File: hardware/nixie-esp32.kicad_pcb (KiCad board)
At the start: 6 copper layers, 70.5 x 70 mm, 53 parts, among them J1 USB4216-03-A_REVA, SW1 RESET, SW2 BOOT, U1 AP7361C-33E-13, U2 ESP32-S3-WROOM-1, U3 SN74AHCT1G125DBVR, U4 SN74141N, U5 SN74141N, U6 SN74141N

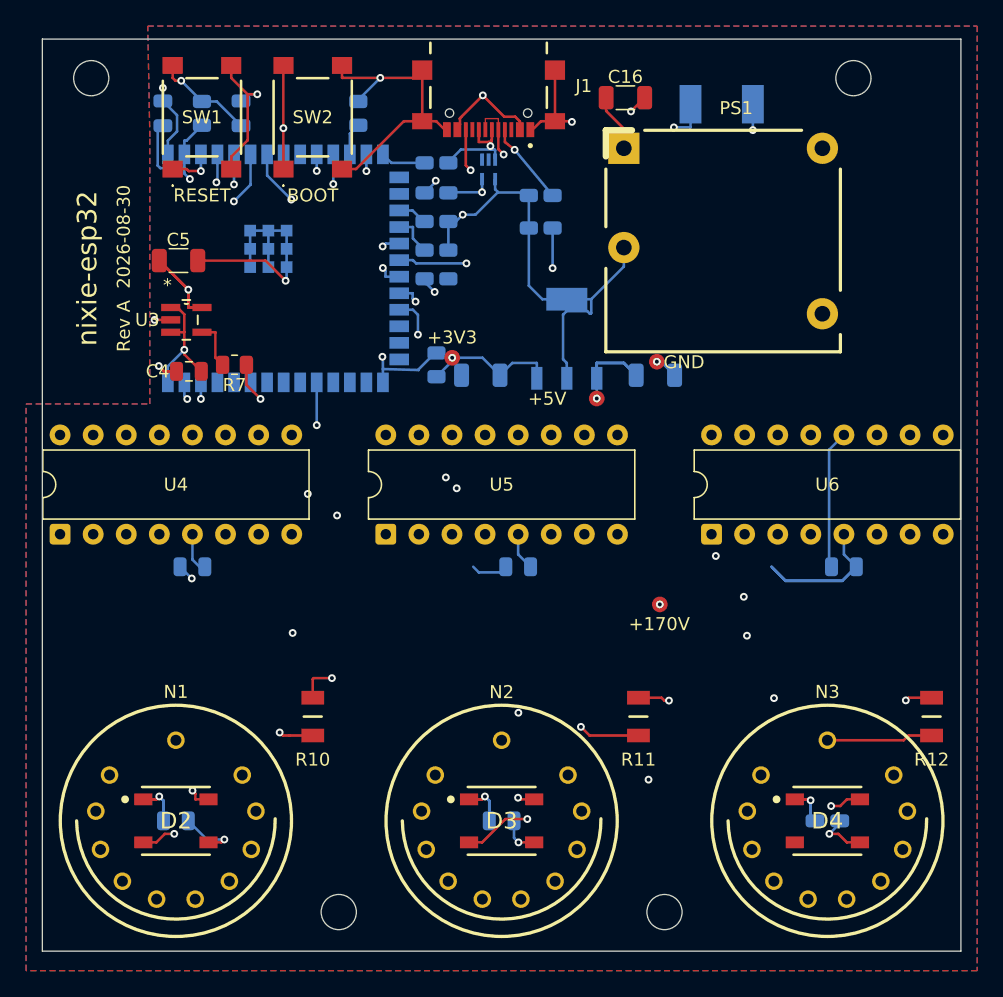
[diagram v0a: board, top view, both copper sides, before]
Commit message: Resolve all DRC warnings
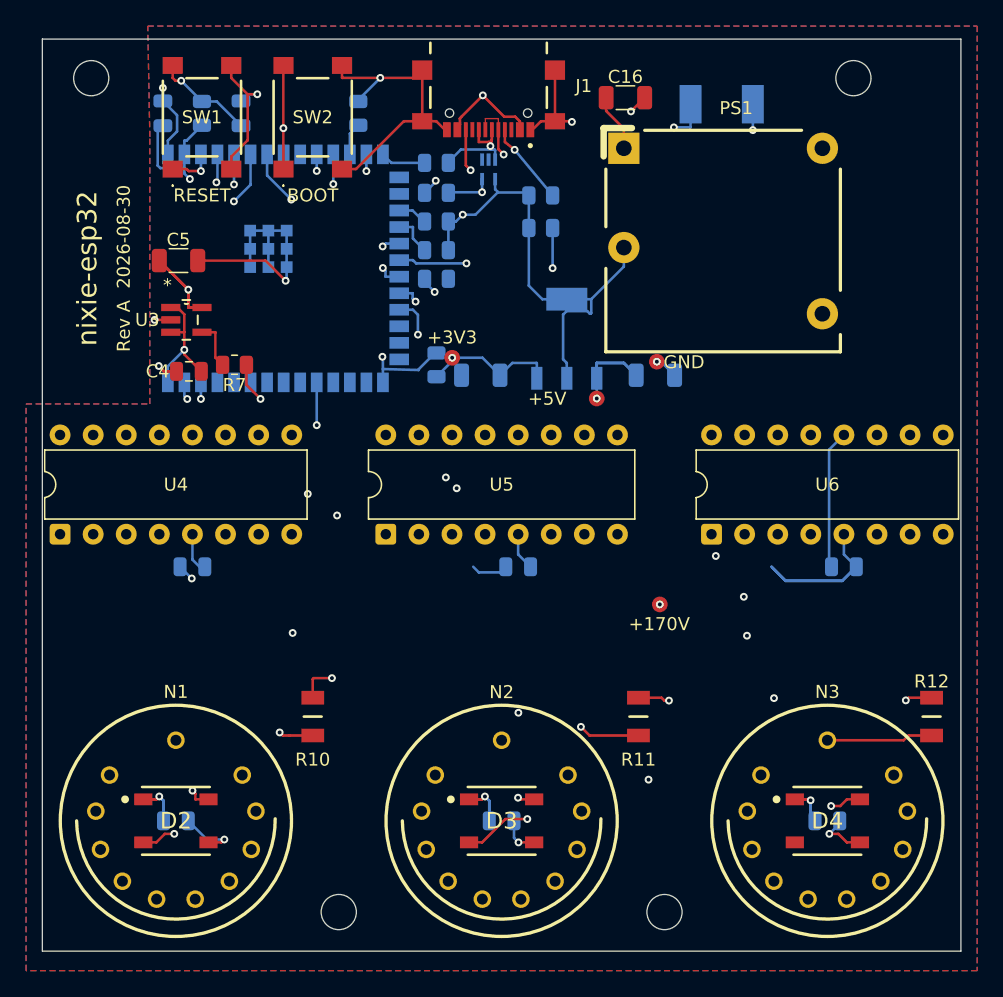
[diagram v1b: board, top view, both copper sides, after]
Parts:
- U4, U6: footprint Package_DIP:DIP-16_W7.62mm -> nixie-esp32:DIP-16_W7.62mm
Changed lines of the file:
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@@
 		(duplicate_pad_numbers_are_jumpers no)
 		(fp_line
-			(start -1.38 -1.38)
-			(end -1.38 0.62)
+			(start -1.55 -1.55)
+			(end -1.55 0.62)
 			(stroke
 				(width 0.5)
@@
 		)
 		(fp_line
-			(start -1.38 -1.38)
-			(end 0.62 -1.38)
+			(start -1.55 -1.55)
+			(end 0.62 -1.55)
 			(stroke
 				(width 0.5)
@@
 		)
 	)
-	(footprint "Package_DIP:DIP-16_W7.62mm"
+	(footprint "nixie-esp32:DIP-16_W7.62mm"
 		(layer "F.Cu")
 		(at 170.11 114.5 90)
@@
 		(duplicate_pad_numbers_are_jumpers no)
 		(fp_line
-			(start 6.46 -1.33)
-			(end 4.81 -1.33)
+			(start 6.46 -1.18)
+			(end 4.81 -1.18)
 			(stroke
 				(width 0.12)
@@
 		)
 		(fp_line
-			(start 2.81 -1.33)
-			(end 1.16 -1.33)
+			(start 2.81 -1.18)
+			(end 1.16 -1.18)
 			(stroke
 				(width 0.12)
@@
 		)
 		(fp_line
-			(start 1.16 -1.33)
-			(end 1.16 19.11)
+			(start 1.16 -1.18)
+			(end 1.16 18.96)
 			(stroke
 				(width 0.12)
@@
 		)
 		(fp_line
-			(start 6.46 19.11)
-			(end 6.46 -1.33)
+			(start 6.46 18.96)
+			(end 6.46 -1.18)
 			(stroke
 				(width 0.12)
@@
 		)
 		(fp_line
-			(start 1.16 19.11)
-			(end 6.46 19.11)
+			(start 1.16 18.96)
+			(end 6.46 18.96)
 			(stroke
 				(width 0.12)
@@
 		)
 		(fp_arc
-			(start 4.81 -1.33)
+			(start 4.81 -1.18)
 			(mid 3.81 -0.33)
-			(end 2.81 -1.33)
+			(end 2.81 -1.18)
 			(stroke
 				(width 0.12)
@@
 		)
 	)
-	(footprint "Package_DIP:DIP-16_W7.62mm"
+	(footprint "nixie-esp32:DIP-16_W7.62mm"
 		(layer "F.Cu")
 		(at 120.11 114.5 90)
@@
 		(duplicate_pad_numbers_are_jumpers no)
 		(fp_line
-			(start 6.46 -1.33)
-			(end 4.81 -1.33)
+			(start 6.46 -1.18)
+			(end 4.81 -1.18)
 			(stroke
 				(width 0.12)
@@
 		)
 		(fp_line
-			(start 2.81 -1.33)
-			(end 1.16 -1.33)
+			(start 2.81 -1.18)
+			(end 1.16 -1.18)
 			(stroke
 				(width 0.12)
@@
 		)
 		(fp_line
-			(start 1.16 -1.33)
-			(end 1.16 19.11)
+			(start 1.16 -1.18)
+			(end 1.16 18.96)
 			(stroke
 				(width 0.12)
@@
 		)
 		(fp_line
-			(start 6.46 19.11)
-			(end 6.46 -1.33)
+			(start 6.46 18.96)
+			(end 6.46 -1.18)
 			(stroke
 				(width 0.12)
@@
 		)
 		(fp_line
-			(start 1.16 19.11)
-			(end 6.46 19.11)
+			(start 1.16 18.96)
+			(end 6.46 18.96)
 			(stroke
 				(width 0.12)
@@
 		)
 		(fp_arc
-			(start 4.81 -1.33)
+			(start 4.81 -1.18)
 			(mid 3.81 -0.33)
-			(end 2.81 -1.33)
+			(end 2.81 -1.18)
 			(stroke
 				(width 0.12)
@@
 		(tags "Resistor")
 		(property "Reference" "R12"
-			(at -3.3 0 0)
+			(at 2.7 0 0)
 			(layer "F.SilkS")
 			(effects
@@
 		)
 		(pad "1" smd roundrect
-			(at -0.95 0 270)
+			(at -0.95 0 90)
 			(size 1 1.45)
 			(layers "B.Cu" "B.Mask" "B.Paste")
@@
 		)
 		(pad "2" smd roundrect
-			(at 0.95 0 270)
+			(at 0.95 0 90)
 			(size 1 1.45)
 			(layers "B.Cu" "B.Mask" "B.Paste")
@@
 		)
 		(pad "1" smd roundrect
-			(at -0.95 0 180)
+			(at -0.95 0)
 			(size 1 1.45)
 			(layers "B.Cu" "B.Mask" "B.Paste")
@@
 		)
 		(pad "2" smd roundrect
-			(at 0.95 0 180)
+			(at 0.95 0)
 			(size 1 1.45)
 			(layers "B.Cu" "B.Mask" "B.Paste")
@@
 		(tags "capacitor")
 		(property "Reference" "C12"
-			(at 0 1.68 0)
+			(at -3.43 0 0)
 			(layer "B.SilkS")
 			(effects
@@
 		(tags "capacitor")
 		(property "Reference" "C11"
-			(at 0 1.68 0)
+			(at -3.429999 0 0)
 			(layer "B.SilkS")
 			(effects
@@
 		(tags "resistor")
 		(property "Reference" "R6"
-			(at -1.5 2.3 0)
+			(at -2.4 0 0)
 			(layer "B.SilkS")
 			(effects
@@
 		)
 		(pad "1" smd roundrect
-			(at -0.9125 0 270)
+			(at -0.9125 0 90)
 			(size 1.025 1.4)
 			(layers "B.Cu" "B.Mask" "B.Paste")
@@
 		)
 		(pad "2" smd roundrect
-			(at 0.9125 0 270)
+			(at 0.9125 0 90)
 			(size 1.025 1.4)
 			(layers "B.Cu" "B.Mask" "B.Paste")
@@
 		)
 		(pad "1" smd roundrect
-			(at -0.9125 0 270)
+			(at -0.9125 0)
 			(size 1.025 1.4)
 			(layers "B.Cu" "B.Mask" "B.Paste")
@@
 		)
 		(pad "2" smd roundrect
-			(at 0.9125 0 270)
+			(at 0.9125 0)
 			(size 1.025 1.4)
 			(layers "B.Cu" "B.Mask" "B.Paste")
@@
 		)
 		(pad "1" smd roundrect
-			(at -0.95 0 270)
+			(at -0.95 0)
 			(size 1 1.45)
 			(layers "B.Cu" "B.Mask" "B.Paste")
@@
 		)
 		(pad "2" smd roundrect
-			(at 0.95 0 270)
+			(at 0.95 0)
 			(size 1 1.45)
 			(layers "B.Cu" "B.Mask" "B.Paste")
@@
 		)
 		(pad "1" smd roundrect
-			(at -0.9125 0 270)
+			(at -0.9125 0)
 			(size 1.025 1.4)
 			(layers "B.Cu" "B.Mask" "B.Paste")
@@
 		)
 		(pad "2" smd roundrect
-			(at 0.9125 0 270)
+			(at 0.9125 0)
 			(size 1.025 1.4)
 			(layers "B.Cu" "B.Mask" "B.Paste")
@@
 		)
 		(pad "1" smd roundrect
-			(at -0.95 0 270)
+			(at -0.95 0 90)
 			(size 1 1.45)
 			(layers "B.Cu" "B.Mask" "B.Paste")
@@
 		)
 		(pad "2" smd roundrect
-			(at 0.95 0 270)
+			(at 0.95 0 90)
 			(size 1 1.45)
 			(layers "B.Cu" "B.Mask" "B.Paste")
@@
 		)
 		(pad "1" smd roundrect
-			(at -0.9125 0 90)
+			(at -0.9125 0)
 			(size 1.025 1.4)
 			(layers "B.Cu" "B.Mask" "B.Paste")
@@
 		)
 		(pad "2" smd roundrect
-			(at 0.9125 0 90)
+			(at 0.9125 0)
 			(size 1.025 1.4)
 			(layers "B.Cu" "B.Mask" "B.Paste")
@@
 			(polygon
 				(pts
-					(xy 126.84 103.1) (xy 126.84 85.1) (xy 117.5 85.1) (xy 117.5 103.1)
+					(xy 126.84 103.1) (xy 126.84 85.1) (xy 120.89 85.1) (xy 120.89 103.1)
 				)
 			)
@@
 		(tags "capacitor")
 		(property "Reference" "C13"
-			(at 0 1.68 0)
+			(at -3.43 0 0)
 			(layer "B.SilkS")
 			(effects
@@
 		)
 		(pad "1" smd roundrect
-			(at -0.95 0 180)
+			(at -0.95 0)
 			(size 1 1.45)
 			(layers "B.Cu" "B.Mask" "B.Paste")
@@
 		)
 		(pad "2" smd roundrect
-			(at 0.95 0 180)
+			(at 0.95 0)
 			(size 1 1.45)
 			(layers "B.Cu" "B.Mask" "B.Paste")
@@
 		)
 		(pad "1" smd roundrect
-			(at -0.9125 0 270)
+			(at -0.9125 0 90)
 			(size 1.025 1.4)
 			(layers "B.Cu" "B.Mask" "B.Paste")
@@
 		)
 		(pad "2" smd roundrect
-			(at 0.9125 0 270)
+			(at 0.9125 0 90)
 			(size 1.025 1.4)
 			(layers "B.Cu" "B.Mask" "B.Paste")
@@
 		)
 		(pad "1" smd roundrect
-			(at -1.475 0 180)
+			(at -1.475 0)
 			(size 1.15 1.8)
 			(layers "B.Cu" "B.Mask" "B.Paste")
@@
 		)
 		(pad "2" smd roundrect
-			(at 1.475 0 180)
+			(at 1.475 0)
 			(size 1.15 1.8)
 			(layers "B.Cu" "B.Mask" "B.Paste")
@@
 		)
 		(pad "1" smd roundrect
-			(at -0.9125 0 90)
+			(at -0.9125 0)
 			(size 1.025 1.4)
 			(layers "B.Cu" "B.Mask" "B.Paste")
@@
 		)
 		(pad "2" smd roundrect
-			(at 0.9125 0 90)
+			(at 0.9125 0)
 			(size 1.025 1.4)
 			(layers "B.Cu" "B.Mask" "B.Paste")
@@
 		)
 		(pad "1" smd roundrect
-			(at -0.9125 0 90)
+			(at -0.9125 0)
 			(size 1.025 1.4)
 			(layers "B.Cu" "B.Mask" "B.Paste")
@@
 		)
 		(pad "2" smd roundrect
-			(at 0.9125 0 90)
+			(at 0.9125 0)
 			(size 1.025 1.4)
 			(layers "B.Cu" "B.Mask" "B.Paste")
@@
 		)
 		(pad "1" smd roundrect
-			(at -0.9125 0 270)
+			(at -0.9125 0)
 			(size 1.025 1.4)
 			(layers "B.Cu" "B.Mask" "B.Paste")
@@
 		)
 		(pad "2" smd roundrect
-			(at 0.9125 0 270)
+			(at 0.9125 0)
 			(size 1.025 1.4)
 			(layers "B.Cu" "B.Mask" "B.Paste")
@@
 		)
 		(pad "1" smd roundrect
-			(at -0.9125 0 90)
+			(at -0.9125 0)
 			(size 1.025 1.4)
 			(layers "B.Cu" "B.Mask" "B.Paste")
@@
 		)
 		(pad "2" smd roundrect
-			(at 0.9125 0 90)
+			(at 0.9125 0)
 			(size 1.025 1.4)
 			(layers "B.Cu" "B.Mask" "B.Paste")
@@
 			)
 		)
+	)
+	(zone
+		(layers "F.Cu" "B.Cu" "In1.Cu" "In2.Cu" "In3.Cu" "In4.Cu")
+		(name "antenna keepout to board edge")
+		(hatch edge 0.5)
+		(connect_pads
+			(clearance 0)
+		)
+		(min_thickness 0.25)
+		(keepout
+			(tracks not_allowed)
+			(vias not_allowed)
+			(pads not_allowed)
+			(copperpour not_allowed)
+			(footprints allowed)
+		)
+		(placement
+			(enabled no)
+			(sheetname "")
+		)
+		(fill
+			(thermal_gap 0.5)
+			(thermal_bridge_width 0.5)
+			(island_removal_mode 0)
+		)
+		(polygon
+			(pts
+				(xy 117.5 85.1) (xy 120.89 85.1) (xy 120.89 103.1) (xy 117.5 103.1)
+			)
+		)

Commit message: Add component values and context labels to silkscreen
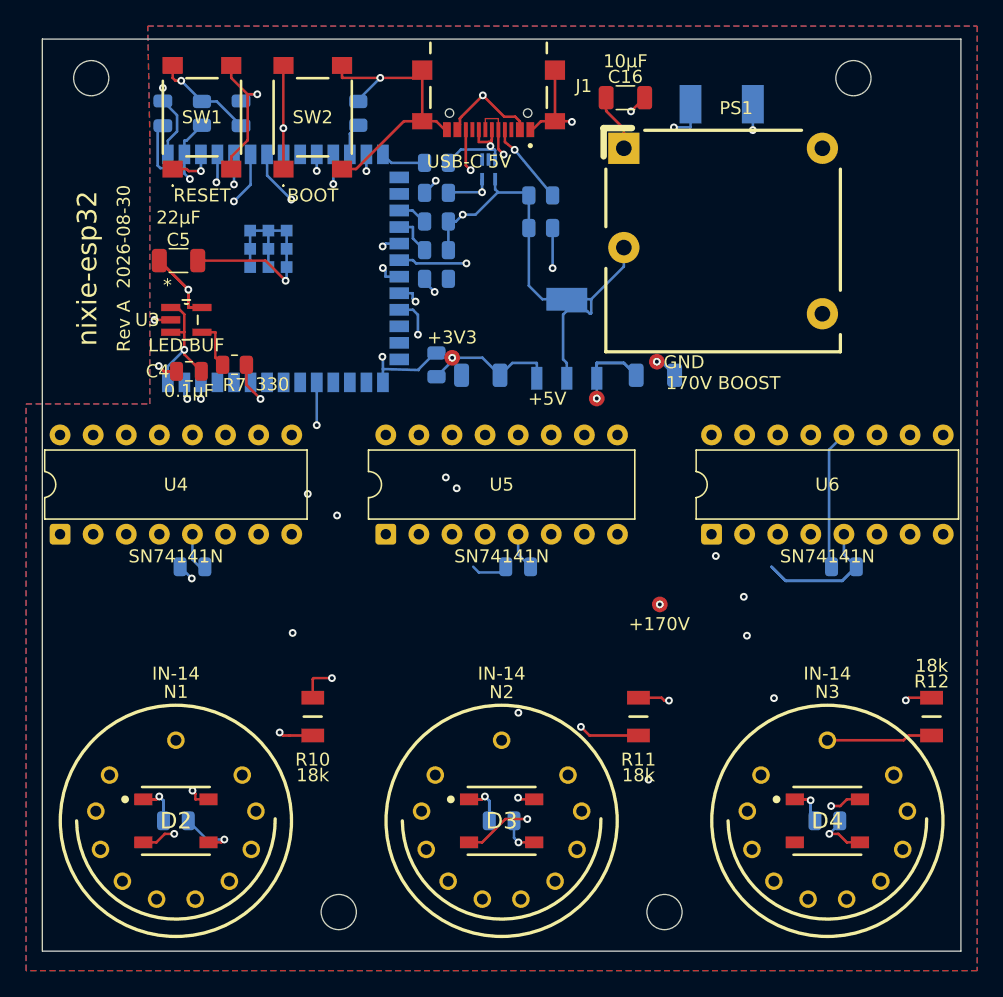
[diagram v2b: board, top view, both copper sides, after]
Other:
- board text added: "1.5A PTC"
- board text added: "170V BOOST"
- board text added: "3V3"
- board text added: "3x 10k"
- board text added: "ESD"
- board text added: "LED BUF"
- board text added: "USB-C 5V"
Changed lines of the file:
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@@
 		)
 		(property "Value" "SN74141N"
-			(at 3.81 20.11 90)
-			(layer "F.Fab")
+			(at -1.7 8.89 0)
+			(layer "F.SilkS")
 			(effects
 				(font
@@
 		)
 		(property "Value" "SN74141N"
-			(at 3.81 20.11 90)
-			(layer "F.Fab")
+			(at -1.7 8.89 0)
+			(layer "F.SilkS")
 			(effects
 				(font
@@
 		)
 		(property "Value" "SN74141N"
-			(at 3.81 20.11 90)
-			(layer "F.Fab")
+			(at -1.7 8.89 0)
+			(layer "F.SilkS")
 			(effects
 				(font
@@
 		)
 		(property "Value" "18k"
-			(at 0 0 90)
+			(at -4.5 0 0)
 			(layer "F.SilkS")
-			(hide yes)
 			(effects
 				(font
-					(size 1.27 1.27)
-					(thickness 0.254)
+					(size 1 1)
+					(thickness 0.15)
 				)
 			)
@@
 		)
 		(property "Value" "18k"
-			(at 0 0 90)
+			(at -4.5 0 0)
 			(layer "F.SilkS")
-			(hide yes)
 			(effects
 				(font
-					(size 1.27 1.27)
-					(thickness 0.254)
+					(size 1 1)
+					(thickness 0.15)
 				)
 			)
@@
 		)
 		(property "Value" "330"
-			(at 0 1.65 0)
-			(layer "F.Fab")
+			(at 2.9 1.5 0)
+			(layer "F.SilkS")
 			(effects
 				(font
@@
 		)
 		(property "Value" "0.1µF"
-			(at 0 1.68 0)
-			(layer "F.Fab")
+			(at 0 1.5 0)
+			(layer "F.SilkS")
 			(effects
 				(font
@@
 		)
 		(property "Value" "10µF"
-			(at 0 1.85 0)
-			(layer "F.Fab")
+			(at 0 -2.8 0)
+			(layer "F.SilkS")
 			(effects
 				(font
@@
 		)
 		(property "Value" "IN-14"
-			(at 0 0 0)
-			(layer "F.Fab")
+			(at 0 11.3 0)
+			(layer "F.SilkS")
 			(effects
 				(font
-					(size 1.27 1.27)
+					(size 1 1)
+					(thickness 0.15)
 				)
 			)
@@
 		)
 		(property "Value" "18k"
-			(at 0 0 90)
+			(at 3.9 0 0)
 			(layer "F.SilkS")
-			(hide yes)
 			(effects
 				(font
-					(size 1.27 1.27)
-					(thickness 0.254)
+					(size 1 1)
+					(thickness 0.15)
 				)
 			)
@@
 		)
 		(property "Value" "IN-14"
-			(at 0 0 0)
-			(layer "F.Fab")
+			(at 0 11.3 0)
+			(layer "F.SilkS")
 			(effects
 				(font
-					(size 1.27 1.27)
+					(size 1 1)
+					(thickness 0.15)
 				)
 			)
@@
 		)
 		(property "Value" "22µF"
-			(at 0 1.85 0)
-			(layer "F.Fab")
+			(at -0.000001 -3.3 0)
+			(layer "F.SilkS")
 			(effects
 				(font
@@
 		)
 		(property "Value" "IN-14"
-			(at 0 0 0)
-			(layer "F.Fab")
+			(at 0 11.3 0)
+			(layer "F.SilkS")
 			(effects
 				(font
-					(size 1.27 1.27)
+					(size 1 1)
+					(thickness 0.15)
 				)
 			)
@@
 		)
 		(property "Value" "1µF"
-			(at 0 -1.68 90)
-			(layer "B.Fab")
+			(at 2.3 3.3 0)
+			(layer "B.SilkS")
 			(effects
 				(font
@@
 		)
 		(property "Value" "10µF"
-			(at 0 -1.85 0)
-			(layer "B.Fab")
+			(at 0 -2.8 0)
+			(layer "B.SilkS")
 			(effects
 				(font
@@
 		)
 		(property "Value" "0.1µF"
-			(at 0 -1.68 0)
-			(layer "B.Fab")
+			(at 0 3.4 0)
+			(layer "B.SilkS")
 			(effects
 				(font
@@
 		)
 		(property "Value" "0.1µF"
-			(at 0 -1.68 0)
-			(layer "B.Fab")
+			(at -3.73 -1.6 0)
+			(layer "B.SilkS")
 			(effects
 				(font
@@
 		)
 		(property "Value" "0.1µF"
-			(at 0 -1.68 0)
-			(layer "B.Fab")
+			(at -3.73 -1.6 0)
+			(layer "B.SilkS")
 			(effects
 				(font
@@
 		)
 		(property "Value" "10k"
-			(at 0 -1.65 90)
-			(layer "B.Fab")
+			(at -3.6 0 0)
+			(layer "B.SilkS")
 			(effects
 				(font
@@
 		)
 		(property "Value" "10k"
-			(at 0 -1.65 90)
+			(at 5.15 0 0)
 			(layer "B.Fab")
+			(hide yes)
 			(effects
 				(font
@@
 		)
 		(property "Value" "10k"
-			(at 0 -1.65 90)
-			(layer "B.Fab")
+			(at 4 1.199999 0)
+			(layer "B.SilkS")
 			(effects
 				(font
@@
 		)
 		(property "Value" "0.1µF"
-			(at 0 -1.68 90)
-			(layer "B.Fab")
+			(at 0 3.4 0)
+			(layer "B.SilkS")
 			(effects
 				(font
@@
 		(tags "Integrated Circuit")
 		(property "Reference" "D1"
-			(at 0 -2.5 0)
+			(at -1.8 -1.1 0)
 			(layer "B.SilkS")
 			(effects
@@
 		)
 		(property "Value" "10k"
-			(at 0 -1.65 90)
+			(at 5.15 0 0)
 			(layer "B.Fab")
+			(hide yes)
 			(effects
 				(font
@@
 		)
 		(property "Value" "0.1µF"
-			(at 0 -1.68 90)
-			(layer "B.Fab")
+			(at 4 -0.7 0)
+			(layer "B.SilkS")
 			(effects
 				(font
@@
 		)
 		(property "Value" "5.1k"
-			(at 0 -1.65 90)
-			(layer "B.Fab")
+			(at 2.6 1.6 0)
+			(layer "B.SilkS")
 			(effects
 				(font
@@
 		)
 		(property "Value" "0.1µF"
-			(at 0 -1.68 0)
-			(layer "B.Fab")
+			(at -3.73 -1.6 0)
+			(layer "B.SilkS")
 			(effects
 				(font
@@
 		)
 		(property "Value" "0.1µF"
-			(at 0 -1.68 0)
-			(layer "B.Fab")
+			(at 0 3.4 0)
+			(layer "B.SilkS")
 			(effects
 				(font
@@
 		)
 		(property "Value" "10k"
-			(at 0 -1.65 90)
-			(layer "B.Fab")
+			(at 2.3 2.9 0)
+			(layer "B.SilkS")
 			(effects
 				(font
@@
 		)
 		(property "Value" "10µF"
-			(at 0 -1.85 0)
-			(layer "B.Fab")
+			(at 0 2.8 0)
+			(layer "B.SilkS")
 			(effects
 				(font
@@
 		)
 		(property "Value" "22"
-			(at 0 -1.65 90)
-			(layer "B.Fab")
+			(at 5.5 0.6 0)
+			(layer "B.SilkS")
 			(effects
 				(font
@@
 		)
 		(property "Value" "5.1k"
-			(at 0 -1.65 90)
-			(layer "B.Fab")
+			(at 2 -1.6 0)
+			(layer "B.SilkS")
 			(effects
 				(font
@@
 		)
 		(property "Value" "10k"
-			(at 0 -1.65 90)
+			(at 5.15 0 0)
 			(layer "B.Fab")
+			(hide yes)
 			(effects
 				(font
@@
 		)
 		(property "Value" "22"
-			(at 0 -1.65 90)
-			(layer "B.Fab")
+			(at 2.9 -2.4 0)
+			(layer "B.SilkS")
 			(effects
 				(font
@@
 		(layer "Edge.Cuts")
 	)
+	(gr_text "LED BUF"
+		(at 129.8 100 0)
+		(layer "F.SilkS")
+		(effects
+			(font
+				(size 1 1)
+				(thickness 0.15)
+			)
+		)
+	)
 	(gr_text "+3V3"
 		(at 150.2 99.4 0)
@@
 		)
 	)
+	(gr_text "USB-C 5V"
+		(at 151.5 85.9 0)
+		(layer "F.SilkS")
+		(effects
+			(font
+				(size 1 1)
+				(thickness 0.15)
+			)
+		)
+	)
 	(gr_text "+5V"
 		(at 157.5 104.1 0)
@@
 		)
 	)
+	(gr_text "170V BOOST"
+		(at 171 102.9 0)
+		(layer "F.SilkS")
+		(effects
+			(font
+				(size 1 1)
+				(thickness 0.15)
+			)
+		)
+	)
 	(gr_text "Rev A  2026-08-30"
 		(at 125 94.1 90)
@@
 		)
 	)
+	(gr_text "3x 10k"
+		(at 152.9 96.5 0)
+		(layer "B.SilkS")
+		(effects
+			(font
+				(size 1 1)
+				(thickness 0.15)
+			)
+			(justify mirror)
+		)
+	)
 	(gr_text "JLCJLCJLCJLC"
 		(at 154 145.3 0)
 		(layer "B.SilkS")
 		(effects
+			(font
+				(size 1 1)
+				(thickness 0.15)
+			)
+			(justify mirror)
+		)
+	)
+	(gr_text "ESD"
+		(at 155.6 86.35 0)
+		(layer "B.SilkS")
+		(effects
+			(font
+				(size 1 1)
+				(thickness 0.15)
+			)
+			(justify mirror)
+		)
+	)
+	(gr_text "3V3"
+		(at 161.8 104.4 0)
+		(layer "B.SilkS")
+		(effects
+			(font
+				(size 1 1)
+				(thickness 0.15)
+			)
+			(justify mirror)
+		)
+	)
+	(gr_text "1.5A PTC"
+		(at 172.5 84.4 0)
+		(layer "B.SilkS")
+		(effects
